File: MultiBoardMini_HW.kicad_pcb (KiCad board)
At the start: 2 copper layers, 63 x 63 mm, 58 parts, among them J1 PB0, J2 PA10, J3 Conn_01x02_Male, J4 PA10, J6 Conn_01x04, SW1 PF1, SW2 RESET, SW3 SW_Push_DPDT, SW5 SW_Push_DPDT, T3 PTS_1.5_2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

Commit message: MOT配線見直し
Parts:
- removed REF4 (x4): MountingHole_3.2mm_M3, MountingHole:MountingHole_3.2mm_M3
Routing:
- net GND: track 215.2 -> 190.1 mm

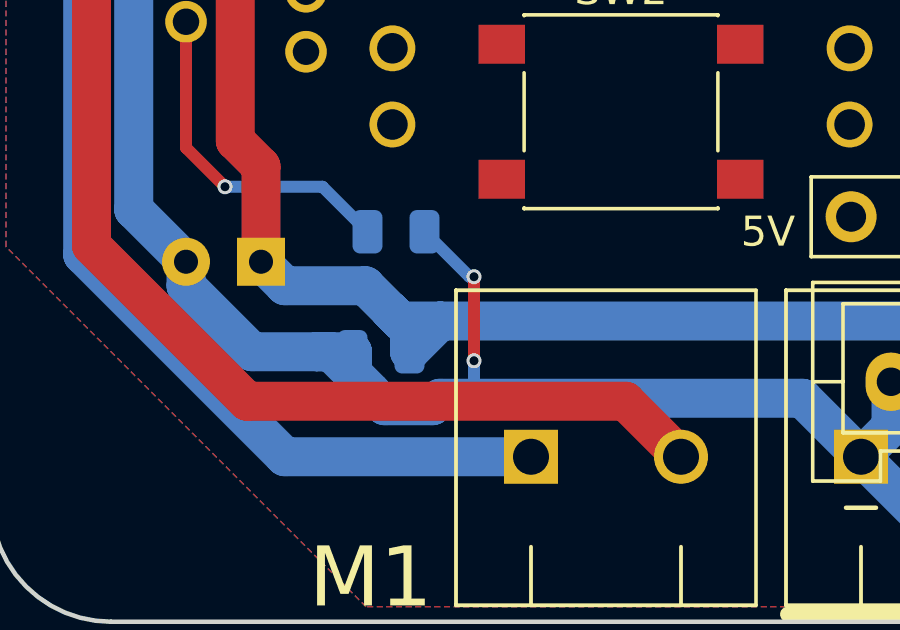
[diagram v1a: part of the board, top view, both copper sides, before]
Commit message: MDGND配線見直し
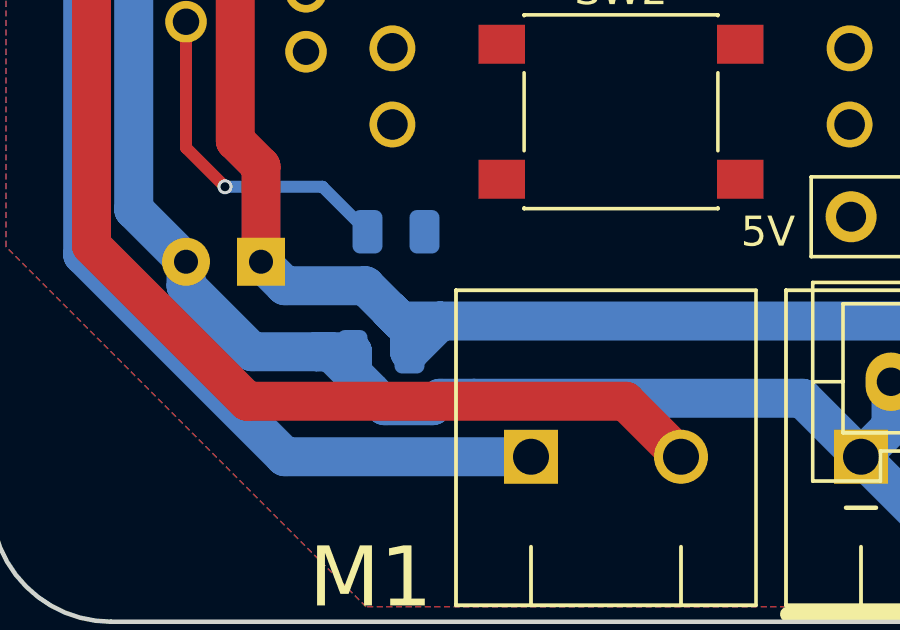
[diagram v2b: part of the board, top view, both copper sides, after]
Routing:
- net GND: track 190.1 -> 183.8 mm, vias 2 -> 0
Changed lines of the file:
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@@
   (segment (start 16.155 -7.35) (end 16.155 -6.6) (width 0.4) (layer "F.Cu") (net 2))
   (segment (start 7.5 -10.7) (end 6.5 -10.7) (width 1.3) (layer "F.Cu") (net 2))
-  (segment (start -15.4 20) (end -15.4 22.8) (width 0.4) (layer "F.Cu") (net 2))
   (segment (start 15.505 -8) (end 16.155 -7.35) (width 0.4) (layer "F.Cu") (net 2))
   (segment (start 4.96 3.84) (end 5.3 3.5) (width 1.3) (layer "F.Cu") (net 2))
@@
   (segment (start 6.25 -10.45) (end 6.5 -10.7) (width 1.3) (layer "F.Cu") (net 2))
   (segment (start 5.3 2.775) (end 6.25 1.825) (width 1.3) (layer "F.Cu") (net 2))
-  (via (at -15.4 22.8) (size 0.5) (drill 0.3) (layers "F.Cu" "B.Cu") (free) (net 2))
-  (via (at -15.4 20) (size 0.5) (drill 0.3) (layers "F.Cu" "B.Cu") (free) (net 2))
   (segment (start 19.45 23.225) (end 19.45 22.5) (width 1.3) (layer "B.Cu") (net 2))
   (segment (start -26.744 6.55) (end -25.694 5.5) (width 1.3) (layer "B.Cu") (net 2))
   (segment (start -4.45 24.05) (end -15.4 24.05) (width 1.3) (layer "B.Cu") (net 2))
   (segment (start -2.5 26) (end -0.55493 27.94507) (width 1.3) (layer "B.Cu") (net 2))
-  (segment (start -15.4 22.8) (end -15.4 24.05) (width 0.4) (layer "B.Cu") (net 2))
   (segment (start 25 11.52) (end 24.95 11.47) (width 1.3) (layer "B.Cu") (net 2))
   (segment (start 20.95 -4.5) (end 20.95 -7.53) (width 1.3) (layer "B.Cu") (net 2))
@@
   (segment (start 19.206 3.52) (end 19.206 8.4) (width 1.3) (layer "B.Cu") (net 2))
   (segment (start 20.95 2.47) (end 20.95 -4.5) (width 1.3) (layer "B.Cu") (net 2))
-  (segment (start -15.55 20) (end -17.05 18.5) (width 0.4) (layer "B.Cu") (net 2))
   (segment (start -21 7.3) (end -21 5.7) (width 1.3) (layer "B.Cu") (net 2))
   (segment (start -16.786522 24.3) (end -18.375 24.3) (width 1.3) (layer "B.Cu") (net 2))
@@
   (segment (start 18.4 24.275) (end 19.45 23.225) (width 1.3) (layer "B.Cu") (net 2))
   (segment (start -19.45 23.225) (end -19.45 22.5) (width 1.3) (layer "B.Cu") (net 2))
-  (segment (start -15.4 20) (end -15.55 20) (width 0.4) (layer "B.Cu") (net 2))
   (segment (start 19.206 8.4) (end 19.206 10.6) (width 1.3) (layer "B.Cu") (net 2))
   (segment (start -21 6.5) (end -21 7.3) (width 1.3) (layer "B.Cu") (net 2))

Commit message: 配線完成
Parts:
- added REF**: MountingHole_3.2mm_M3, MountingHole:MountingHole_3.2mm_M3, F.Cu at (27.5, -27.5)
- added REF**: MountingHole_3.2mm_M3, MountingHole:MountingHole_3.2mm_M3, F.Cu at (-27.5, 27.5)
- added REF**: MountingHole_3.2mm_M3, MountingHole:MountingHole_3.2mm_M3, F.Cu at (-27.5, -27.5)
- added REF**: MountingHole_3.2mm_M3, MountingHole:MountingHole_3.2mm_M3, F.Cu at (27.5, 27.5)
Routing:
- net GND: track 183.8 -> 423.1 mm
- net +3V3: track 7.48 -> 145.1 mm, vias 0 -> 2
- net +5V: track 20.1 -> 141.0 mm, vias 0 -> 2
- net Net-(U2A-PB1): track 0.00 -> 90.2 mm, vias 0 -> 3
- net Net-(U2B-PA5): track 0.00 -> 50.7 mm, vias 0 -> 4
- net Net-(U2A-PA8): track 0.00 -> 50.4 mm, vias 0 -> 2
- net Net-(U2B-PB3): track 0.00 -> 46.3 mm
- net Net-(ENC/IO_2-Pin_3): track 0.00 -> 44.6 mm, vias 0 -> 2
- net Net-(U2A-NRST_1): track 0.00 -> 44.5 mm, vias 0 -> 1
- net Net-(U2A-PB4): track 0.00 -> 43.8 mm, vias 0 -> 2
- net Net-(U2A-PB0): track 0.00 -> 39.8 mm
- net Net-(ENC/IO_2-Pin_4): track 0.00 -> 38.9 mm, vias 0 -> 3
- net Net-(D1-A): track 0.00 -> 37.4 mm, vias 0 -> 2
- net Net-(J6-Pin_1): track 0.00 -> 35.8 mm, vias 0 -> 3
- net Net-(J6-Pin_2): track 0.00 -> 34.6 mm, vias 0 -> 3
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
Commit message: ほぼ完成
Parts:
- moved D2 8.47 mm to (9.50, 3.00), turned to 90 degrees
- moved C2 0.39 mm to (10.2, -9.25)
- renumbered PWR1 to PWR
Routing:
- net GND: track 423.1 -> 418.2 mm
- net +5V: track 141.0 -> 144.7 mm
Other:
- board text added: "10kΩ"
- board text added: "120Ω"
- board text added: "47μF"
- board text added: "51kΩ"
- board text added: "5V PWR"
- board text added: "6-32V"
- board text added: "CAN"
- board text added: "ESP BOOT"
- board text added: "ESP EN"
- board text added: "ESP32 WROOM 32E"
- board text added: "H"
- board text added: "L"
- board text added: "M1 ON"
- board text added: "M2 ON"
- board text added: "MCP2562"
- board text added: "MultiBoardMini Ver0.41 UGOKU Lab 2023-11"
- board text added: "Nucleo F303K8"
- board text added: "PB3"
- board text added: "PF1"
- board text added: "RESET"
- board text added: "SERVO"
- board text removed: "DL"
- board text removed: "MultiBoardMini Ver0.41 UGOKU Lab 2023-10"

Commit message: V0.41試作発注用完成 PCB ASSEMBLY用BOM、positionデータ追加
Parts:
- removed D2: D, Diode_SMD:D_SOD-123F
- SW1, SW2: footprint Button_Switch_SMD:SW_Push_1P1T_NO_6x6mm_H9.5mm -> MultiBoardMini_Libraries:SW_TL3301FF160QG
- renumbered PWR to L1, PA7 to L2, PA6 to L3
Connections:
- C1 pad 1: +5V -> GND
- C10 pad 1: +5V -> GND
- J4 pad 3: +5V -> GND
- J6 pad 4: +5V -> GND
- JP1 pad 3: +5V -> GND
- JP2 pad 3: +5V -> GND
- JP3 pad 3: +5V -> GND
- JP4 pad 3: +5V -> GND
- U1 pad 3: +5V -> GND
- U2 pad 4_1: +5V -> GND
- U2 pad 4_4: +5V -> GND
- U6 pad 3: +5V -> GND
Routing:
- net GND: track 418.2 -> 566.7 mm, vias 0 -> 2
- net +5V: track 144.7 -> 0.00 mm, vias 2 -> 0
- net Net-(U2B-PB3): track 46.3 -> 54.4 mm
- net Net-(U2A-NRST_1): track 44.5 -> 40.8 mm
- net Net-(U2A-PF1): track 27.8 -> 24.9 mm
- net Net-(U2A-PB5): track 30.3 -> 30.9 mm
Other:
- board text added: "3.3μF"
- board text added: "PWR"
- board text removed: "4.7μF"

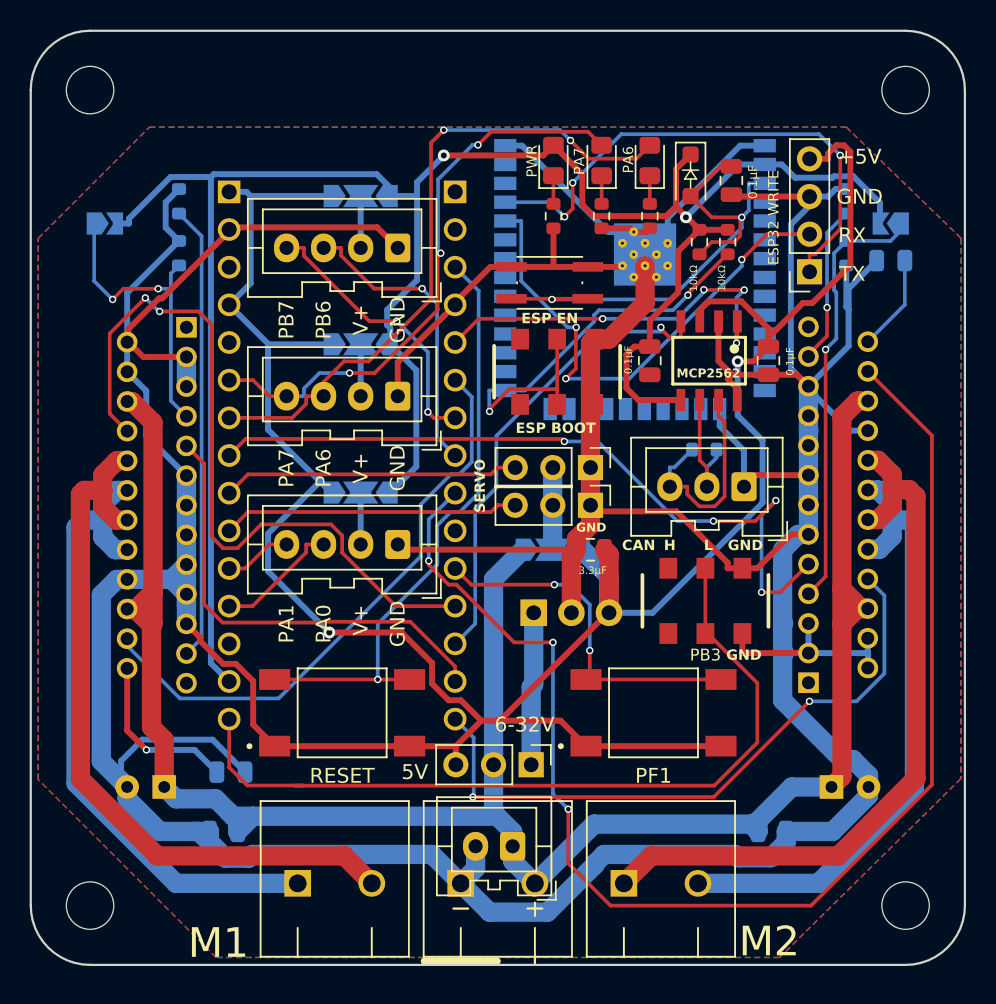
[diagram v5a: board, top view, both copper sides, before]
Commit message: GNDと5V+がつながっていた問題を解消
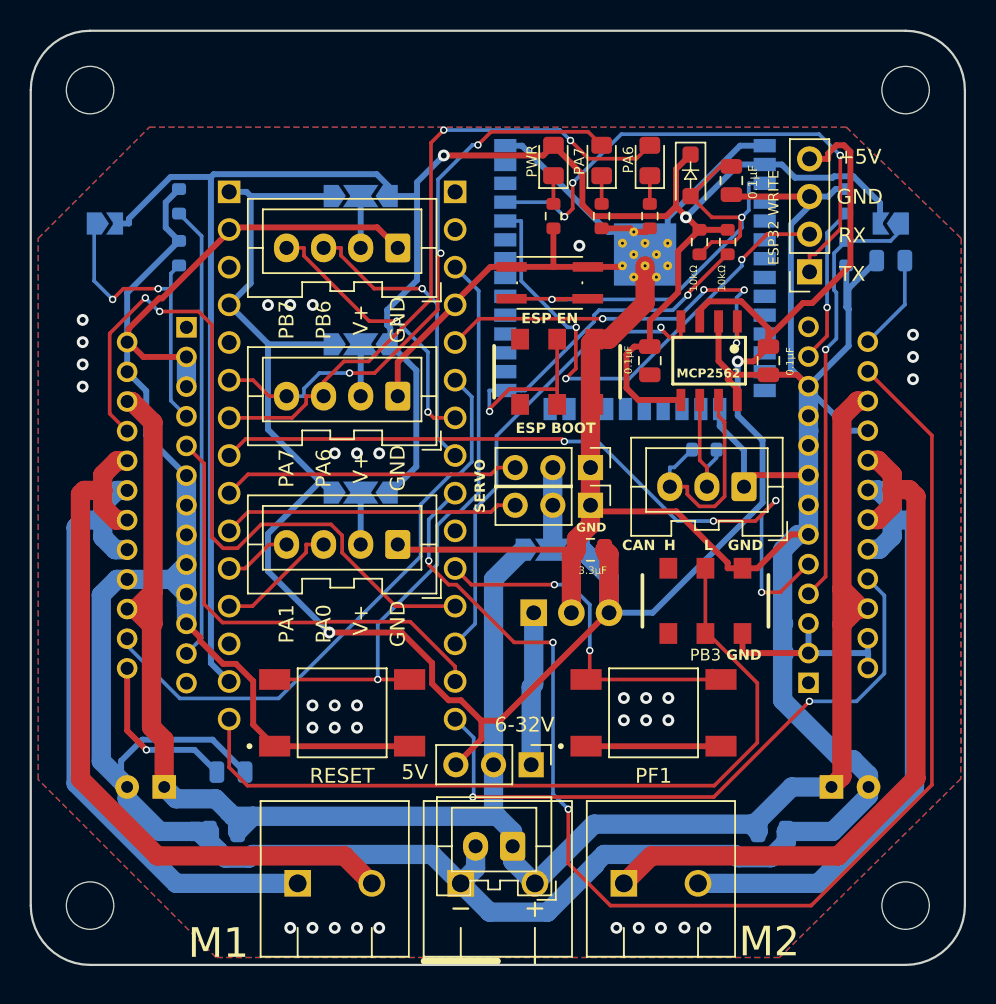
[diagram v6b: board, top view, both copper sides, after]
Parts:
- C10: value 4.7μF -> 3.3μF
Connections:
- C1 pad 1: GND -> +5V
- C10 pad 1: GND -> +5V
- J4 pad 3: GND -> +5V
- J6 pad 4: GND -> +5V
- JP1 pad 3: GND -> +5V
- JP2 pad 3: GND -> +5V
- JP3 pad 3: GND -> +5V
- JP4 pad 3: GND -> +5V
- U1 pad 3: GND -> +5V
- U2 pad 4_1: GND -> +5V
- U2 pad 4_4: GND -> +5V
- U6 pad 3: GND -> +5V
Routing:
- net GND: track 566.7 -> 416.7 mm, vias 2 -> 36
- net +5V: track 0.00 -> 140.1 mm, vias 0 -> 2
- net Net-(U2B-PB3): track 54.4 -> 53.9 mm
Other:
- board text added: "MultiBoardMini Ver0.42 UGOKU Lab 2024-1"
- board text removed: "MultiBoardMini Ver0.41 UGOKU Lab 2023-11"

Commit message: ESPとNucleoが接続されてなかったので接続
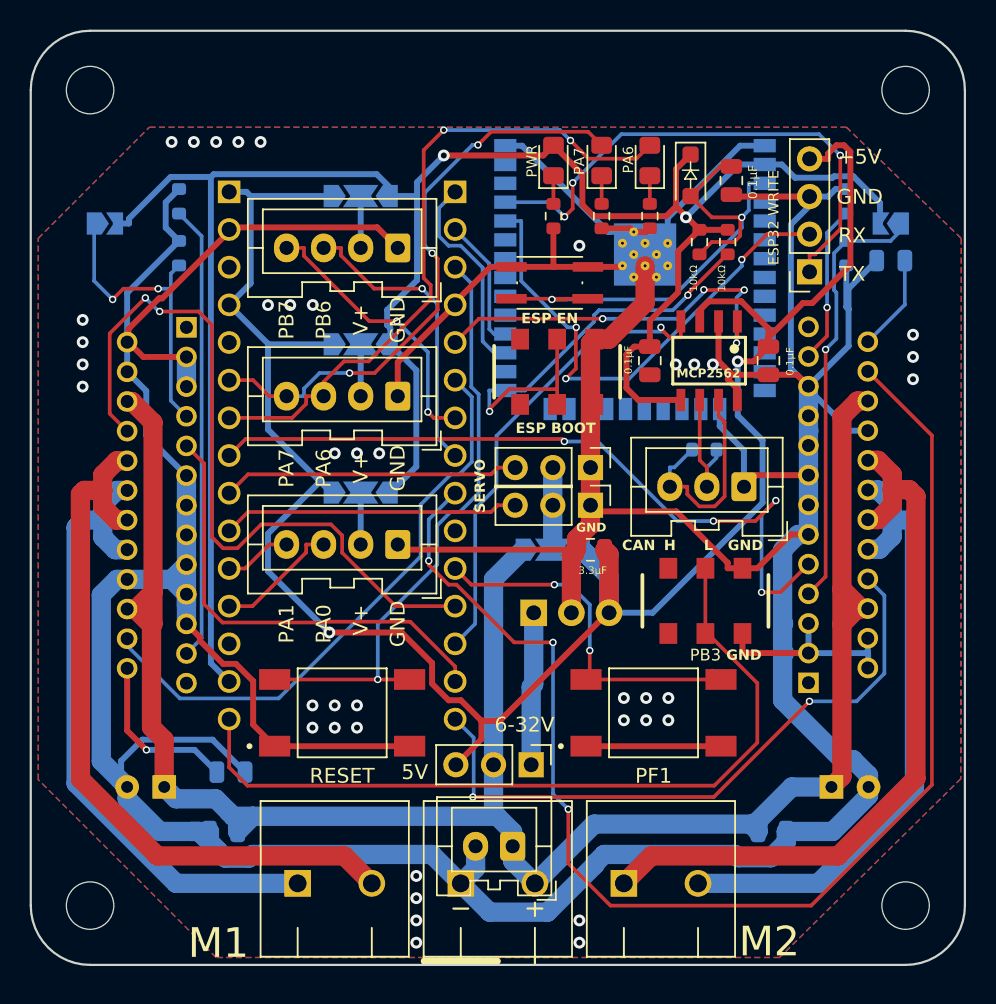
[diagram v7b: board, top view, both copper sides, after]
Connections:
- U2 pad 3_1: rx -> Net-(U2A-PA9)
- U2 pad 3_2: tx -> Net-(U2A-PA10)
- U7 pad 27: unconnected-(U7-IO16-Pad27) -> Net-(U2A-PA9)
- U7 pad 28: unconnected-(U7-IO17-Pad28) -> Net-(U2A-PA10)
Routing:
- net Net-(U2A-PA9): track 0.00 -> 14.1 mm
- net Net-(U2A-PA10): track 0.00 -> 8.88 mm
- net Net-(ENC/IO_2-Pin_4): track 38.9 -> 39.5 mm
- net GND: vias 36 -> 40
